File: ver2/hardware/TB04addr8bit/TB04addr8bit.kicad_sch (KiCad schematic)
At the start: 16 parts, among them J1 USB_C_Receptacle_PowerOnly_6P, SW1 SW_SPDT, U13 74LS157, U15 74HC138, U16 74HC00, U32 74AHC04, U42 74AHC04

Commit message: ver2: 回路図の要修正5件を修正しアノテーションを掛け直し
- 74HC193(旧U39/新U38)の~CO・~BOをVDD直結から開放に(出力短絡の回避)
- 電源未接続だった4IC(74HC00/74LS32/74AHC04/74LS08)にVCC/GNDを配線
  し、バイパスコンデンサ0.1u×4を追加
- ネット名 Decord を DCR に統一(デコーダ制御信号のラッチ不成立を解消)
- PC_LAOD の綴りを PC_LOAD に修正
- 書込デコーダ138の入力を OPR8-10 から sel_a0-2 へ付け替え
  (LD Ri,[Im8] が別レジスタに書く不具合の解消)
- ver1基板由来だった参照記号をアノテーション掛け直しで整理
  (部品216個・名前付きネット146本とも掛け直し前後で一致、ERCも同数)
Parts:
- renumbered C35 to C1, C26 to C2, C1 to C3, C7 to C4, C25 to C5, D21 to D1, R6 to R1, R7 to R2, R9 to R3, U32 to U1, U42 to U2, U13 to U3, U15 to U4, U16 to U5
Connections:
- net OPR10: no longer U4.3 (A2)
- net OPR8: no longer U4.1 (A0)
- net OPR9: no longer U4.2 (A1)
- net sel_a0: now also U4.1 (A0)
- net sel_a1: now also U4.2 (A1)
- net sel_a2: now also U4.3 (A2)
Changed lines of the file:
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@@
 		)
 	)
-	(global_label "OPR9"
+	(global_label "sel_a1"
 		(shape input)
 		(at 267.97 132.08 180)
@@
 		)
 	)
-	(global_label "OPR8"
+	(global_label "sel_a0"
 		(shape input)
 		(at 267.97 129.54 180)
@@
 		)
 	)
-	(global_label "OPR10"
+	(global_label "sel_a2"
 		(shape input)
 		(at 267.97 134.62 180)
@@
 		(dnp no)
 		(fields_autoplaced yes)
-		(property "Reference" "#PWR011"
+		(property "Reference" "#PWR09"
 			(at 161.29 233.68 0)
 			(hide yes)
@@
 			(project "TB04addr8bit"
 				(path "/d176c79b-dced-4d01-bcec-7dfd676fcfc2"
-					(reference "#PWR011")
+					(reference "#PWR09")
 					(unit 1)
 				)
@@
 		(dnp no)
 		(fields_autoplaced yes)
-		(property "Reference" "U16"
+		(property "Reference" "U5"
 			(at 167.64 209.5499 0)
 			(show_name no)
@@
 			(project "TB04addr8bit"
 				(path "/d176c79b-dced-4d01-bcec-7dfd676fcfc2"
-					(reference "U16")
+					(reference "U5")
 					(unit 5)
 				)
@@
 		(in_pos_files yes)
 		(dnp no)
-		(property "Reference" "R7"
+		(property "Reference" "R2"
 			(at 77.47 123.19 0)
 			(show_name no)
@@
 			(project "TB04addr8bit"
 				(path "/d176c79b-dced-4d01-bcec-7dfd676fcfc2"
-					(reference "R7")
+					(reference "R2")
 					(unit 1)
 				)
@@
 		(dnp no)
 		(fields_autoplaced yes)
-		(property "Reference" "#PWR01"
+		(property "Reference" "#PWR03"
 			(at 39.37 134.62 0)
 			(hide yes)
@@
 			(project "TB04addr8bit"
 				(path "/d176c79b-dced-4d01-bcec-7dfd676fcfc2"
-					(reference "#PWR01")
+					(reference "#PWR03")
 					(unit 1)
 				)
@@
 		(in_pos_files yes)
 		(dnp no)
-		(property "Reference" "C7"
+		(property "Reference" "C4"
 			(at 63.5 163.83 0)
 			(show_name no)
@@
 			(project "TB04addr8bit"
 				(path "/d176c79b-dced-4d01-bcec-7dfd676fcfc2"
-					(reference "C7")
+					(reference "C4")
 					(unit 1)
 				)
@@
 		(dnp no)
 		(fields_autoplaced yes)
-		(property "Reference" "#FLG02"
+		(property "Reference" "#FLG01"
 			(at 44.45 155.575 0)
 			(hide yes)
@@
 			(project "TB04addr8bit"
 				(path "/d176c79b-dced-4d01-bcec-7dfd676fcfc2"
-					(reference "#FLG02")
+					(reference "#FLG01")
 					(unit 1)
 				)
@@
 		(dnp no)
 		(fields_autoplaced yes)
-		(property "Reference" "#FLG01"
+		(property "Reference" "#FLG02"
 			(at 40.64 165.735 0)
 			(hide yes)
@@
 			(project "TB04addr8bit"
 				(path "/d176c79b-dced-4d01-bcec-7dfd676fcfc2"
-					(reference "#FLG01")
+					(reference "#FLG02")
 					(unit 1)
 				)
@@
 		(in_pos_files yes)
 		(dnp no)
-		(property "Reference" "#PWR07"
+		(property "Reference" "#PWR02"
 			(at 274.32 121.92 0)
 			(hide yes)
@@
 			(project "TB04addr8bit"
 				(path "/d176c79b-dced-4d01-bcec-7dfd676fcfc2"
-					(reference "#PWR07")
+					(reference "#PWR02")
 					(unit 1)
 				)
@@
 		(dnp no)
 		(fields_autoplaced yes)
-		(property "Reference" "C1"
+		(property "Reference" "C3"
 			(at 53.34 165.1 0)
 			(show_name no)
@@
 			(project "TB04addr8bit"
 				(path "/d176c79b-dced-4d01-bcec-7dfd676fcfc2"
-					(reference "C1")
+					(reference "C3")
 					(unit 1)
 				)
@@
 		(in_pos_files yes)
 		(dnp no)
-		(property "Reference" "R9"
+		(property "Reference" "R3"
 			(at 87.63 165.1 0)
 			(show_name no)
@@
 			(project "TB04addr8bit"
 				(path "/d176c79b-dced-4d01-bcec-7dfd676fcfc2"
-					(reference "R9")
+					(reference "R3")
 					(unit 1)
 				)
@@
 		(dnp no)
 		(fields_autoplaced yes)
-		(property "Reference" "C25"
+		(property "Reference" "C5"
 			(at 182.88 209.5499 0)
 			(show_name no)
@@
 			(project "TB04addr8bit"
 				(path "/d176c79b-dced-4d01-bcec-7dfd676fcfc2"
-					(reference "C25")
+					(reference "C5")
 					(unit 1)
 				)
@@
 		(in_pos_files yes)
 		(dnp no)
-		(property "Reference" "#PWR065"
+		(property "Reference" "#PWR06"
 			(at 194.31 173.99 0)
 			(hide yes)
@@
 			(project "TB04addr8bit"
 				(path "/d176c79b-dced-4d01-bcec-7dfd676fcfc2"
-					(reference "#PWR065")
+					(reference "#PWR06")
 					(unit 1)
 				)
@@
 		(dnp no)
 		(fields_autoplaced yes)
-		(property "Reference" "#PWR02"
+		(property "Reference" "#PWR04"
 			(at 66.04 134.62 0)
 			(hide yes)
@@
 			(project "TB04addr8bit"
 				(path "/d176c79b-dced-4d01-bcec-7dfd676fcfc2"
-					(reference "#PWR02")
+					(reference "#PWR04")
 					(unit 1)
 				)
@@
 		(dnp no)
 		(fields_autoplaced yes)
-		(property "Reference" "#PWR08"
+		(property "Reference" "#PWR05"
 			(at 289.56 161.29 0)
 			(hide yes)
@@
 			(project "TB04addr8bit"
 				(path "/d176c79b-dced-4d01-bcec-7dfd676fcfc2"
-					(reference "#PWR08")
+					(reference "#PWR05")
 					(unit 1)
 				)
@@
 		(in_pos_files yes)
 		(dnp no)
-		(property "Reference" "#PWR064"
+		(property "Reference" "#PWR01"
 			(at 179.07 119.38 0)
 			(hide yes)
@@
 			(project "TB04addr8bit"
 				(path "/d176c79b-dced-4d01-bcec-7dfd676fcfc2"
-					(reference "#PWR064")
+					(reference "#PWR01")
 					(unit 1)
 				)
@@
 		(in_pos_files yes)
 		(dnp no)
-		(property "Reference" "U42"
+		(property "Reference" "U2"
 			(at 198.12 62.23 0)
 			(show_name no)
@@
 			(project "TB04addr8bit"
 				(path "/d176c79b-dced-4d01-bcec-7dfd676fcfc2"
-					(reference "U42")
+					(reference "U2")
 					(unit 1)
 				)
@@
 		(in_pos_files yes)
 		(dnp no)
-		(property "Reference" "R6"
+		(property "Reference" "R1"
 			(at 69.85 123.19 0)
 			(show_name no)
@@
 			(project "TB04addr8bit"
 				(path "/d176c79b-dced-4d01-bcec-7dfd676fcfc2"
-					(reference "R6")
+					(reference "R1")
 					(unit 1)
 				)
@@
 		(dnp no)
 		(fields_autoplaced yes)
-		(property "Reference" "D21"
+		(property "Reference" "D1"
 			(at 87.63 176.8474 90)
 			(show_name no)
@@
 			(project "TB04addr8bit"
 				(path "/d176c79b-dced-4d01-bcec-7dfd676fcfc2"
-					(reference "D21")
+					(reference "D1")
 					(unit 1)
 				)
@@
 		(dnp no)
 		(fields_autoplaced yes)
-		(property "Reference" "#PWR04"
+		(property "Reference" "#PWR08"
 			(at 83.82 190.5 0)
 			(hide yes)
@@
 			(project "TB04addr8bit"
 				(path "/d176c79b-dced-4d01-bcec-7dfd676fcfc2"
-					(reference "#PWR04")
+					(reference "#PWR08")
 					(unit 1)
 				)
@@
 		(dnp no)
 		(fields_autoplaced yes)
-		(property "Reference" "C26"
+		(property "Reference" "C2"
 			(at 283.21 105.41 90)
 			(show_name no)
@@
 			(project "TB04addr8bit"
 				(path "/d176c79b-dced-4d01-bcec-7dfd676fcfc2"
-					(reference "C26")
+					(reference "C2")
 					(unit 1)
 				)
@@
 		(dnp no)
 		(fields_autoplaced yes)
-		(property "Reference" "U13"
+		(property "Reference" "U3"
 			(at 196.4533 115.57 0)
 			(show_name no)
@@
 			(project "TB04addr8bit"
 				(path "/d176c79b-dced-4d01-bcec-7dfd676fcfc2"
-					(reference "U13")
+					(reference "U3")
 					(unit 1)
 				)
@@
 		(dnp no)
 		(fields_autoplaced yes)
-		(property "Reference" "#PWR03"
+		(property "Reference" "#PWR07"
 			(at 60.96 181.61 0)
 			(hide yes)
@@
 			(project "TB04addr8bit"
 				(path "/d176c79b-dced-4d01-bcec-7dfd676fcfc2"
-					(reference "#PWR03")
+					(reference "#PWR07")
 					(unit 1)
 				)
@@
 		(dnp no)
 		(fields_autoplaced yes)
-		(property "Reference" "C35"
+		(property "Reference" "C1"
 			(at 187.96 102.87 90)
 			(show_name no)
@@
 			(project "TB04addr8bit"
 				(path "/d176c79b-dced-4d01-bcec-7dfd676fcfc2"
-					(reference "C35")
+					(reference "C1")
 					(unit 1)
 				)
@@
 		(in_pos_files yes)
 		(dnp no)
-		(property "Reference" "U32"
+		(property "Reference" "U1"
 			(at 195.58 41.91 0)
 			(show_name no)
@@
 			(project "TB04addr8bit"
 				(path "/d176c79b-dced-4d01-bcec-7dfd676fcfc2"
-					(reference "U32")
+					(reference "U1")
 					(unit 5)
 				)
@@
 		(dnp no)
 		(fields_autoplaced yes)
-		(property "Reference" "U15"
+		(property "Reference" "U4"
 			(at 291.7033 121.92 0)
 			(show_name no)
@@
 			(project "TB04addr8bit"
 				(path "/d176c79b-dced-4d01-bcec-7dfd676fcfc2"
-					(reference "U15")
+					(reference "U4")
 					(unit 1)
 				)

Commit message: ver2: SPのCU/CDに相ゲートを追加、74HC00の電源ユニットを置き直し
- CU=NAND(DCR, SP_CU&!(SP==7)) / CD=NAND(EXE, SP_CD&(SP!=0)) とし、
  74HC193をアイドルHigh・相の終わりの立ち上がりで1回だけ数える形に変更
  (POP/RETはDCR末のpre-inc、PUSH/CALLはEXE末のpost-dec)
  従来のAND直結ではPUSHがpre-decになり、連続PUSH/POPで
  レベルが継続して2回目のカウントを取りこぼす問題があった
- 空いていた74HC00(U5)の2ゲートを使用。spシートのERCが6件減少
- 74HC00の電源ユニット(U5E)をver1由来の残骸ごと削除しsp側へ置き直し
  (ルートに (project "" reference "U16") が残り電源ユニット未配置扱いだった)
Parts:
- removed C5: 0.1u, Capacitor_THT:C_Disc_D4.3mm_W1.9mm_P5.00mm, symbol Device:C
- removed U5: 74HC00, Package_DIP:DIP-14_W7.62mm_Socket, symbol 74xx:74HC00

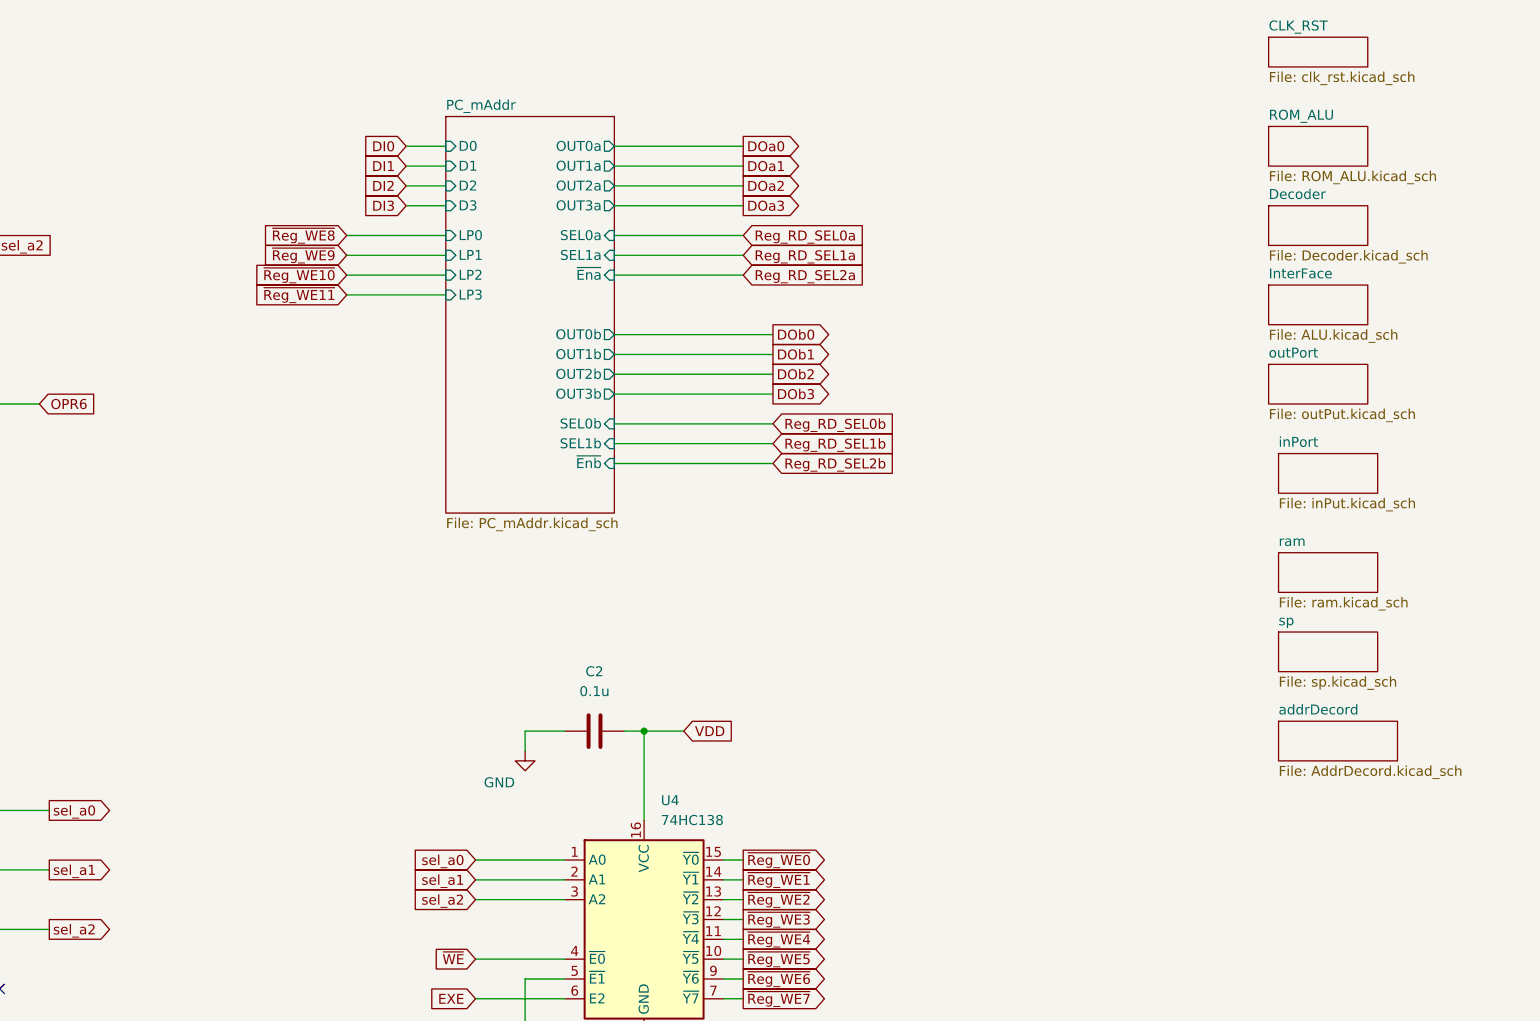
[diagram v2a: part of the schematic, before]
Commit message: ver2: addrMUXシートを新設、リセット起点をFCH1へ、mAddr専用レジスタを廃止
- addrMUX.kicad_sch を新設。74HC138(U41)で SEL_M からアドレス源の
  イネーブルをワンホット生成し、74HC244×5(U42-U46)を配置
  mAddr用(U43)の入力は byte2ラッチのOPR4-11から直取り
- mAddr専用レジスタ(IC11/IC12)を削除。byte2ラッチが mAddr を兼ねる
  これまで消費先ゼロだった OPR7/OPR11 の浮きも解消
- 74HC238の出力割付を1つ回してリセット起点を EXE から FCH1 へ
  (Y0=FCH1/Y1=FCH2/Y2=DCR/Y3=EXE、相順は不変)
- PCの161はCEPを共通イネーブルに揃え、桁上げをTC->CETで接続

未了: 命令ラッチの取り込みエッジを1相ずらす変更(U20 Cp=FCH2 /
U26 Cp=DCR)。EXE中はアドレスバスがmAddrのため、現状のままでは
EXE->FCH1の境目でROMのアクセスが間に合わない
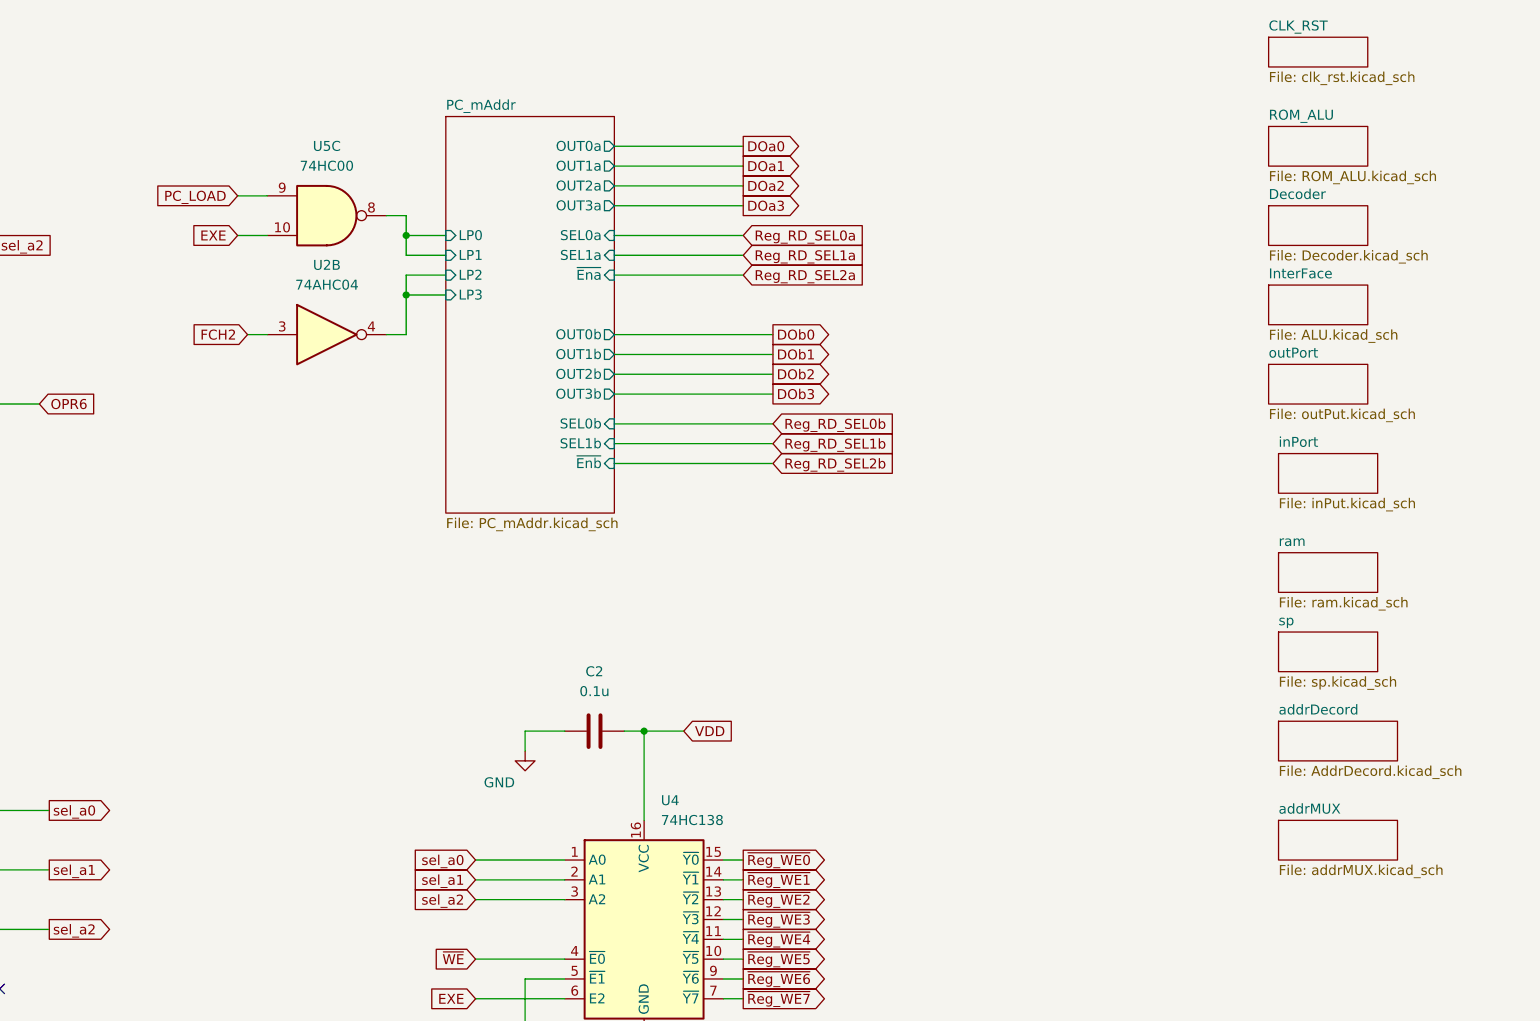
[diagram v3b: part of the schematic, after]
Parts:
- added unit 2 of U2
- added U5: 74HC00, symbol 74xx:74HC00
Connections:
- net EXE: now also U5.10
- new net FCH2: U2.3
- new net PC_LOAD: U5.9
- new net PC_mAddr/LP0: U5.8
- new net PC_mAddr/LP2: U2.4
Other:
- added sheet addrMUX (addrMUX.kicad_sch)
- sheet PC_mAddr ports: added none; removed D0, D1, D2, D3
